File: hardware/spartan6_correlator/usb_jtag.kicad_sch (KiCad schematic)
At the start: 4 parts, among them J1 JST_SHL_SM08B, J2 USB_C_Receptacle_USB2.0_16P, U6 FT2232D, U7 93LCxxB

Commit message: Updates. Lots of them
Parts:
- removed U7: 93LCxxB, symbol Memory_EEPROM:93LCxxB
- added C32, C33, C34: 100n, symbol Device:C
- added C35, C36: 15pF, symbol Device:C
- added D2: D_Schottky, Diode_SMD:D_SMA, symbol Device:D_Schottky
- added D3, D4: GREEN, symbol Device:LED
- added R10, R12, R9: 68, symbol Device:R
- added R11: 470, symbol Device:R
- added R13, R14: 27, symbol Device:R
- added R15, R16: 5.1k, symbol Device:R
- added R17, R18: 1k, symbol Device:R
- added R19: 10k, symbol Device:R
- added R20: 2.2k, symbol Device:R
- added U9: CAT93C46BVI-GT3, Package_SO:SOIC-8_3.9x4.9mm_P1.27mm, symbol Memory_EEPROM:93CxxB
- added Y2: 6MHZ, Crystal:Crystal_SMD_3225-4Pin_3.2x2.5mm, symbol Device:Crystal
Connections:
- net GND: now reaches J2.A1 (GND), J2.A12 (GND), J2.B1 (GND), J2.B12 (GND)
- net GND: now also J2.S1 (SHIELD), U6.18 (GND), U6.25 (GND), U6.34 (GND), U6.45 (AGND), U6.47 (TEST), U6.9 (GND), C32.2, C33.1, C34.1, C35.1, C36.1, R15.2, R16.2, U9.5 (GND)
- net VBUS: now reaches J2.A4 (VBUS), J2.A9 (VBUS), J2.B4 (VBUS), J2.B9 (VBUS)
- net VBUS: now also C34.2, D2.2 (A)
- net at J2.A5 (CC1): now also R15.1
- net at J2.A6 (D+): now also J2.B6 (D+), R14.1
- net at J2.A7 (D-): now also J2.B7 (D-), R13.1
- net at J2.B5 (CC2): now also R16.1
- net at U6.1 (EECLK): now also U9.2 (SCLK)
- net +3V3: now reaches U6.10 (SI/WUA)
- net +3V3: now also U6.14 (VCCIOA), U6.26 (SI/WUB), U6.31 (VCCIOB), D3.2 (A), D4.2 (A)
- net at U6.2 (EEDATA): now also R20.1, U9.3 (DI)
- net at U6.21 (ADBUS3): now also R12.1
- net TDO: now reaches U6.22 (ADBUS2)
- net at U6.23 (ADBUS1): now also R10.1
- net at U6.24 (ADBUS0): now also R9.1
- net at U6.27 (BCBUS3): now also R18.1
- net at U6.28 (BCBUS2): now also R17.1
- net +5V: now reaches U6.3 (VCC)
- net +5V: now also U6.4 (~{RESET}), U6.42 (VCC), C32.1, D2.1 (K), R11.1, R19.2, U9.8 (VCC)
- net USB_RXD: now reaches U6.39 (BDBUS1)
- net USB_TXD: now reaches U6.40 (BDBUS0)
- net at U6.43 (XTIN): now also C35.2, Y2.2
- net at U6.44 (XTOUT): now also C36.2, Y2.1
- net at U6.46 (AVCC): now also R11.2
- net at U6.48 (EECS): now also U9.1 (CS)
- net at U6.5 (~{RSTOUT}): now also U6.7 (USBDP), R14.2
- net at U6.6 (3V3OUT): now also C33.2
- net at U6.8 (USBDM): now also R13.2
- new net: D4.1 (K), R18.2
- new net: R19.1, R20.2, U9.4 (DO)
- new net: D3.1 (K), R17.2
- new net TCK: R9.2
- new net TDI: R10.2
- new net TMS: R12.2
- no-connect marks 0 -> 19
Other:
- moved on the sheet: J1, J2

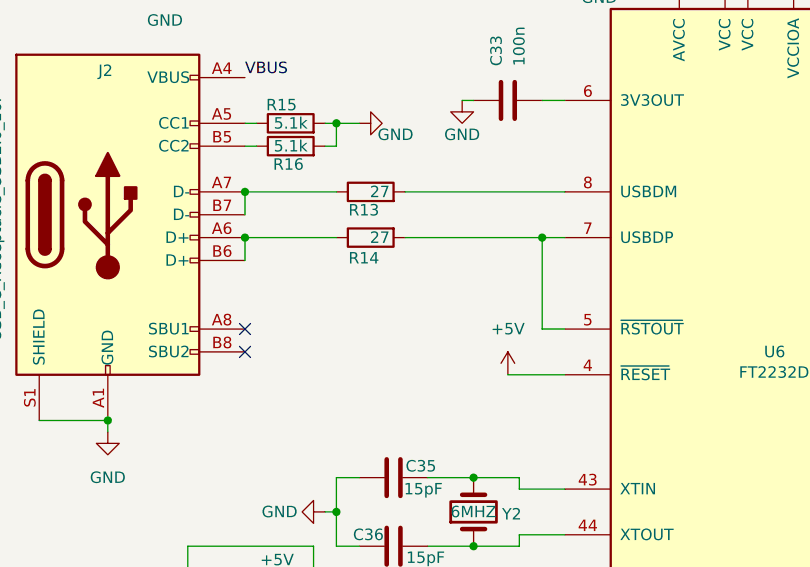
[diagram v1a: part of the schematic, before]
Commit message: Fix SDRAM to correct model
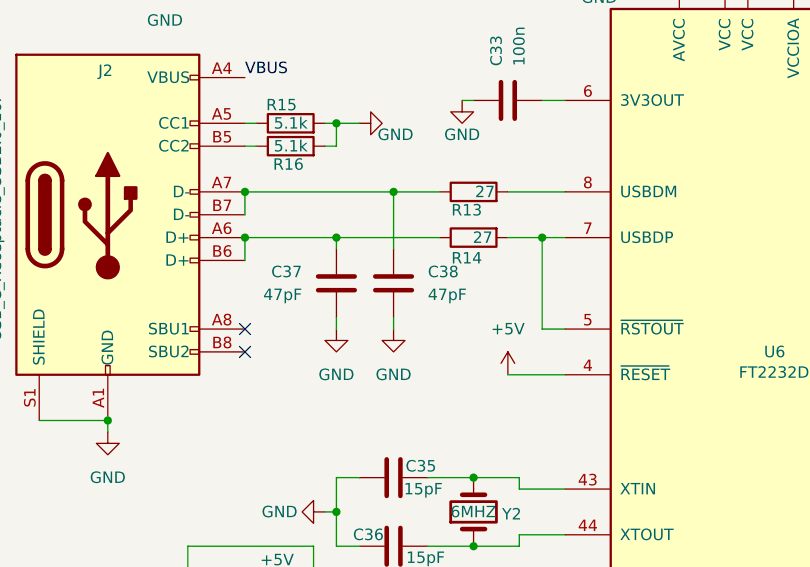
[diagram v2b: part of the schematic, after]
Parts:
- added C37, C38: 47pF, Capacitor_SMD:C_0402_1005Metric, symbol Device:C
- C32, C33, C34, C35, C36: footprint (none) -> Capacitor_SMD:C_0402_1005Metric
- D3, D4: footprint (none) -> LED_SMD:LED_0603_1608Metric
- J2: footprint (none) -> Connector_USB:USB_C_Receptacle_G-Switch_GT-USB-7010ASV
- R10, R11, R12, R13, R14, R15, R16, R17, R18, R19, R20, R9: footprint (none) -> Resistor_SMD:R_0402_1005Metric
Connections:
- net GND: now also C37.2, C38.2
- net at J2.A7 (D-), J2.B7 (D-), R13.1: now also C38.1
- net at J2.A6 (D+), J2.B6 (D+), R14.1: now also C37.1
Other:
- moved on the sheet: R13, R14
